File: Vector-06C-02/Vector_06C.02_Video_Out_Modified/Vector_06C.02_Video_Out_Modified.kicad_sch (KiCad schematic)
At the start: 41 parts, among them J1 DIN-7, U1 74LS08

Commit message: Finalised video mod board design
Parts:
- added R86: R_Variable, symbol Device:R_Variable
- added R95: 1KΩ, symbol Device:R
- added R96, R97, R98: 220Ω, symbol Device:R
- added VT3, VT4, VT5, VT6: 2N3904, Package_TO_SOT_THT:TO-92_Inline, symbol Transistor_BJT:2N3904
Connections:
- net +5V: now also VT4.3 (C), VT5.3 (C), VT6.3 (C)
- net BLUE: now also R98.1, VT6.1 (E); no longer R66.2, R67.2, R70.2, R73.1
- net GND: now also R96.2, R97.2, R98.2, VT3.1 (E)
- net GREEN: now also R97.1, VT5.1 (E); no longer R60.2, R62.2, R64.2, R69.2, R72.1
- net RED: now also R96.1, VT4.1 (E); no longer R55.2, R56.2, R57.2, R68.2, R71.1
- net ~{ССИ}/~{H.SYNC}: now also R95.1
- net at R71.2, R72.2, R73.2: now also VT3.3 (C); no longer D90.6, D90.8
- net COMPOSITE VIDEO: no longer names the net of R50.2, R51.2, R52.2, R53.2, R54.2, R58.2, R59.2, R61.2, R63.2
- net COMPOSITE VIDEO: no longer D56.6, R49.2, R65.2, VT1.2 (B)
- new net: R66.2, R67.2, R70.2, R73.1, VT6.2 (B)
- new net: R55.2, R56.2, R57.2, R68.2, R71.1, VT4.2 (B)
- new net: D56.6, R86.2
- new net: R95.2, VT3.2 (B)
- new net: D90.6, D90.8
- new net: R60.2, R62.2, R64.2, R69.2, R72.1, VT5.2 (B)
- new net ~{C.SYNC}: R49.2, R65.2, R86.1, VT1.2 (B)
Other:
- title: Вектор 06Ц.02 Видеовыход Завода -> Вектор 06Ц.02 Модифицированный Видеовыход
- moved on the sheet: C93, D56D, D74A, D74B, D74C, D74D, D81A, D81B, D81C, D81D, D90B, D90C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

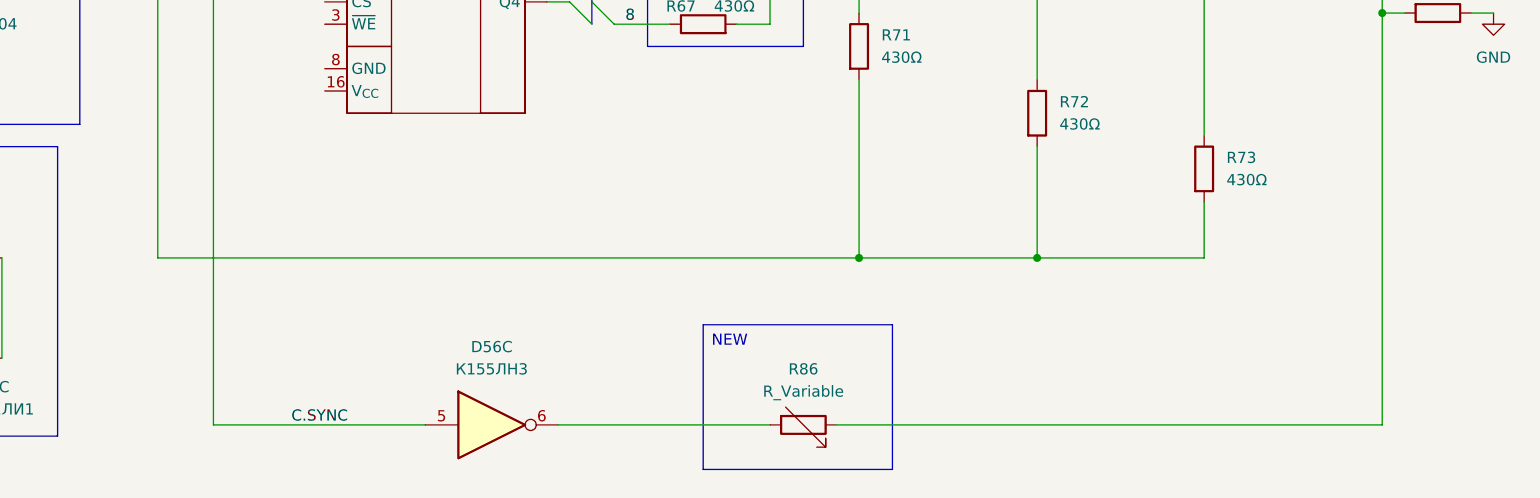
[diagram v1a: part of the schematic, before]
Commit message: Corrected schematic
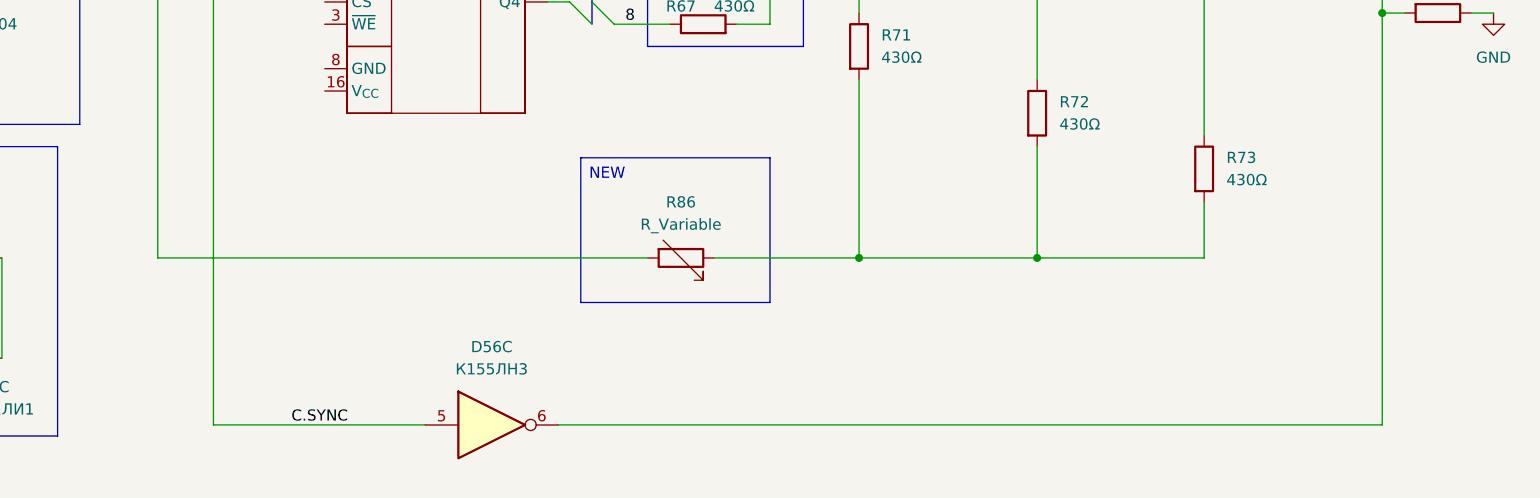
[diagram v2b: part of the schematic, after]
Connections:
- net ~{C.SYNC}: now also D56.6; no longer R86.1
- net at R71.2, R72.2, R73.2: now also R86.1; no longer VT3.3 (C)
- net at R86.2: now also VT3.3 (C); no longer D56.6
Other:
- moved on the sheet: R86
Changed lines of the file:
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@@
 	(text_box "NEW"
 		(exclude_from_sim no)
-		(at 170.18 186.69 0)
+		(at 156.21 167.64 0)
 		(size 21.59 16.51)
 		(margins 0.9525 0.9525 0.9525 0.9525)
@@
 	)
 	(junction
-		(at 187.96 179.07)
+		(at 74.93 184.15)
 		(diameter 0)
 		(color 0 0 0 0)
 	)
 	(junction
-		(at 74.93 184.15)
+		(at 335.28 58.42)
 		(diameter 0)
 		(color 0 0 0 0)
 	)
 	(junction
-		(at 335.28 58.42)
+		(at 187.96 179.07)
 		(diameter 0)
 		(color 0 0 0 0)
@@
 	(wire
 		(pts
-			(xy 185.42 198.12) (xy 247.65 198.12)
-		)
-		(stroke
-			(width 0)
-			(type default)
-		)
-	)
-	(wire
-		(pts
 			(xy 364.49 27.94) (xy 378.46 27.94)
 		)
@@
 	(wire
 		(pts
-			(xy 107.95 179.07) (xy 187.96 179.07)
-		)
-		(stroke
-			(width 0)
-			(type default)
-		)
-	)
-	(wire
-		(pts
 			(xy 152.4 139.7) (xy 154.94 139.7)
 		)
@@
 	(wire
 		(pts
+			(xy 153.67 198.12) (xy 247.65 198.12)
+		)
+		(stroke
+			(width 0)
+			(type default)
+		)
+	)
+	(wire
+		(pts
 			(xy 391.16 27.94) (xy 391.16 29.21)
 		)
@@
 	(wire
 		(pts
+			(xy 171.45 179.07) (xy 187.96 179.07)
+		)
+		(stroke
+			(width 0)
+			(type default)
+		)
+	)
+	(wire
+		(pts
 			(xy 308.61 58.42) (xy 294.64 58.42)
 		)
@@
 	(wire
 		(pts
+			(xy 107.95 179.07) (xy 163.83 179.07)
+		)
+		(stroke
+			(width 0)
+			(type default)
+		)
+	)
+	(wire
+		(pts
 			(xy 173.99 123.19) (xy 180.34 123.19)
 		)
@@
 	(wire
 		(pts
-			(xy 153.67 198.12) (xy 177.8 198.12)
-		)
-		(stroke
-			(width 0)
-			(type default)
-		)
-	)
-	(wire
-		(pts
 			(xy 58.42 184.15) (xy 74.93 184.15)
 		)
@@
 	(symbol
 		(lib_id "Device:R_Variable")
-		(at 181.61 198.12 270)
+		(at 167.64 179.07 270)
 		(unit 1)
 		(exclude_from_sim no)
@@
 		(fields_autoplaced yes)
 		(property "Reference" "R86"
-			(at 181.61 191.77 90)
+			(at 167.64 172.72 90)
 			(effects
 				(font
@@
 		)
 		(property "Value" "R_Variable"
-			(at 181.61 194.31 90)
+			(at 167.64 175.26 90)
 			(effects
 				(font
@@
 		)
 		(property "Footprint" ""
-			(at 181.61 196.342 90)
+			(at 167.64 177.292 90)
 			(effects
 				(font
@@
 		)
 		(property "Datasheet" "~"
-			(at 181.61 198.12 0)
+			(at 167.64 179.07 0)
 			(effects
 				(font
@@
 		)
 		(property "Description" "Variable resistor"
-			(at 181.61 198.12 0)
+			(at 167.64 179.07 0)
 			(effects
 				(font
